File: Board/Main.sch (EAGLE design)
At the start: 1 part

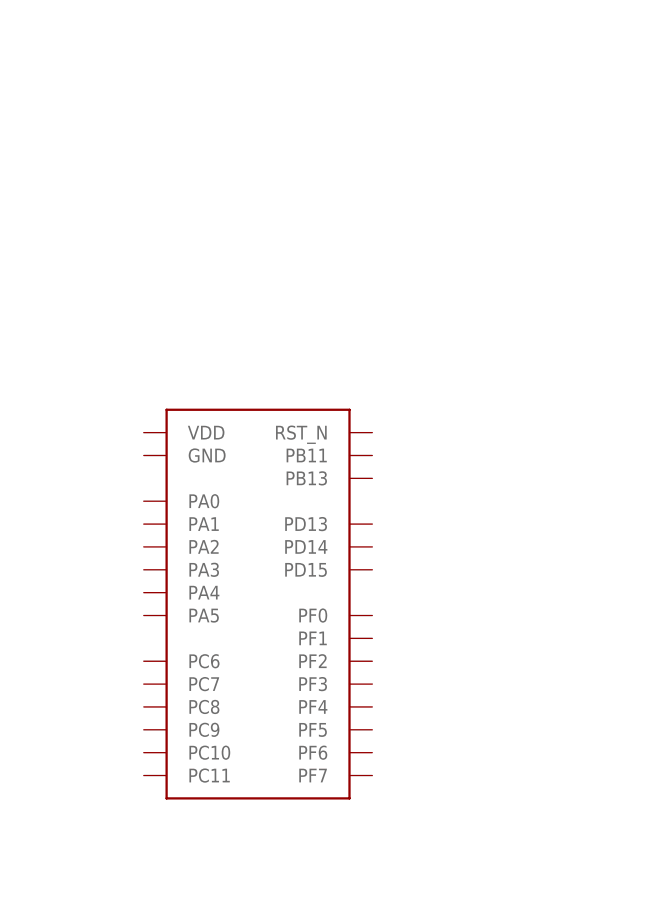
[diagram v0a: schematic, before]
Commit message: Add battery managment
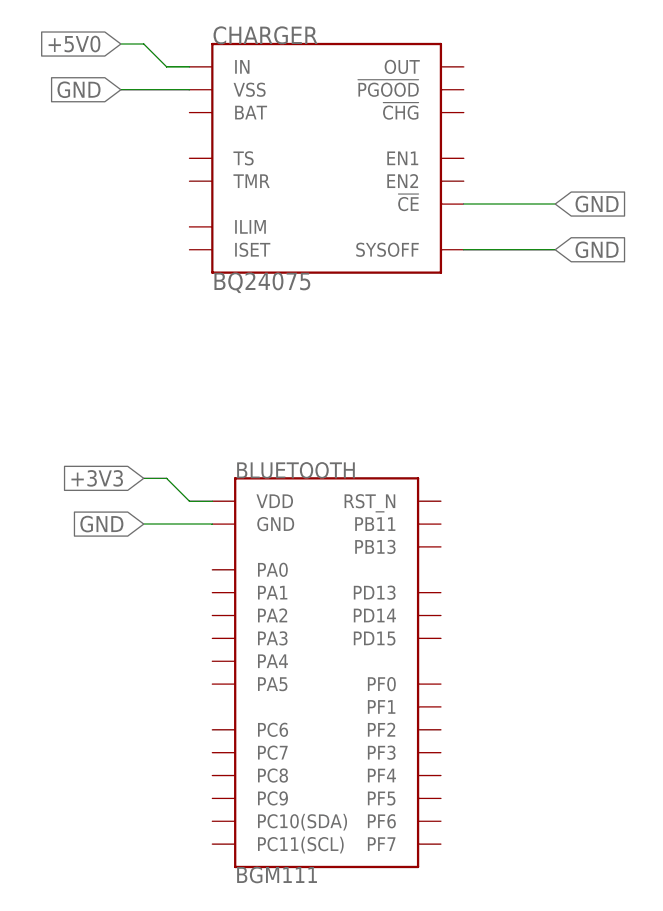
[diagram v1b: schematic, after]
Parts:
- removed BGM111: BGM111, Main Components:BGM111
- added BLUETOOTH: BGM111, Main Components:BGM111
- added CHARGER: BQ24075, Main Components:BQ24075BQ24075
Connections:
- new net +3V3: BLUETOOTH.VDD
- new net +5V0: CHARGER.IN
- new net GND: BLUETOOTH.GND, CHARGER.!CE, CHARGER.SYSOFF, CHARGER.VSS
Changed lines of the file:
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@@
 </classes>
 <parts>
-<part name="BGM111" library="Main Components" deviceset="BGM111" device="" value="BGM111"/>
+<part name="CHARGER" library="Main Components" deviceset="BQ24075" device="BQ24075" value="BQ24075"/>
+<part name="BLUETOOTH" library="Main Components" deviceset="BGM111" device="" value="BGM111"/>
 </parts>
 <sheets>
@@
 </plain>
 <instances>
-<instance part="BGM111" gate="BLUETOOTH" x="48.26" y="58.42" smashed="yes"/>
+<instance part="CHARGER" gate="CHARGER" x="55.88" y="106.68" smashed="yes">
+<attribute name="NAME" x="43.18" y="119.38" size="1.9304" layer="95" font="vector"/>
+<attribute name="VALUE" x="43.18" y="93.98" size="1.9304" layer="96" font="vector" align="top-left"/>
+</instance>
+<instance part="BLUETOOTH" gate="BLUETOOTH" x="55.88" y="50.8" smashed="yes">
+<attribute name="NAME" x="45.72" y="71.12" size="1.778" layer="95" font="vector"/>
+<attribute name="VALUE" x="45.72" y="27.94" size="1.778" layer="96" font="vector" align="top-left"/>
+</instance>
 </instances>
 <busses>
 </busses>
 <nets>
+<net name="GND" class="0">
+<segment>
+<pinref part="BLUETOOTH" gate="BLUETOOTH" pin="GND"/>
+<wire x1="43.18" y1="66.04" x2="35.56" y2="66.04" width="0.1524" layer="91"/>
+<label x="35.56" y="66.04" size="1.778" layer="95" rot="R180" xref="yes"/>
+</segment>
+<segment>
+<pinref part="CHARGER" gate="CHARGER" pin="VSS"/>
+<wire x1="40.64" y1="114.3" x2="33.02" y2="114.3" width="0.1524" layer="91"/>
+<label x="33.02" y="114.3" size="1.778" layer="95" rot="R180" xref="yes"/>
+</segment>
+<segment>
+<pinref part="CHARGER" gate="CHARGER" pin="!CE"/>
+<wire x1="71.12" y1="101.6" x2="81.28" y2="101.6" width="0.1524" layer="91"/>
+<label x="81.28" y="101.6" size="1.778" layer="95" xref="yes"/>
+</segment>
+<segment>
+<pinref part="CHARGER" gate="CHARGER" pin="SYSOFF"/>
+<wire x1="71.12" y1="96.52" x2="81.28" y2="96.52" width="0.1524" layer="91"/>
+<label x="81.28" y="96.52" size="1.778" layer="95" xref="yes"/>
+</segment>
+</net>
+<net name="+3V3" class="0">
+<segment>
+<pinref part="BLUETOOTH" gate="BLUETOOTH" pin="VDD"/>
+<wire x1="43.18" y1="68.58" x2="40.64" y2="68.58" width="0.1524" layer="91"/>
+<wire x1="40.64" y1="68.58" x2="38.1" y2="71.12" width="0.1524" layer="91"/>
+<wire x1="38.1" y1="71.12" x2="35.56" y2="71.12" width="0.1524" layer="91"/>
+<label x="35.56" y="71.12" size="1.778" layer="95" rot="R180" xref="yes"/>
+</segment>
+</net>
+<net name="+5V0" class="0">
+<segment>
+<pinref part="CHARGER" gate="CHARGER" pin="IN"/>
+<wire x1="40.64" y1="116.84" x2="38.1" y2="116.84" width="0.1524" layer="91"/>
+<wire x1="38.1" y1="116.84" x2="35.56" y2="119.38" width="0.1524" layer="91"/>
+<wire x1="35.56" y1="119.38" x2="33.02" y2="119.38" width="0.1524" layer="91"/>
+<label x="33.02" y="119.38" size="1.778" layer="95" rot="R180" xref="yes"/>
+</segment>
+</net>
 </nets>
 </sheet>

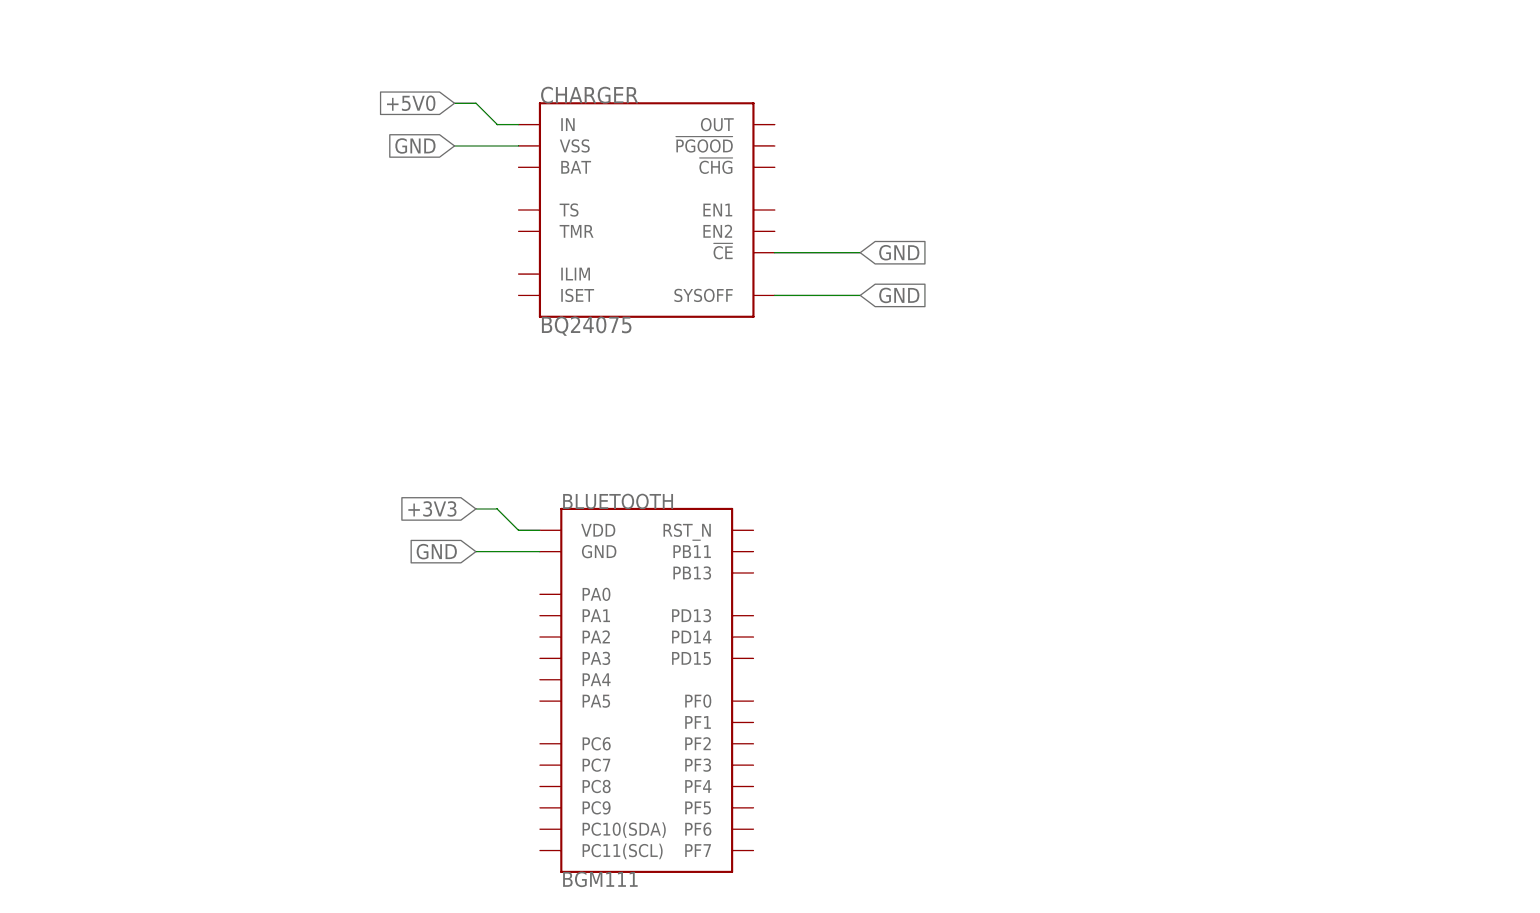
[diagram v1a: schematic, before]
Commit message: Add motor driver
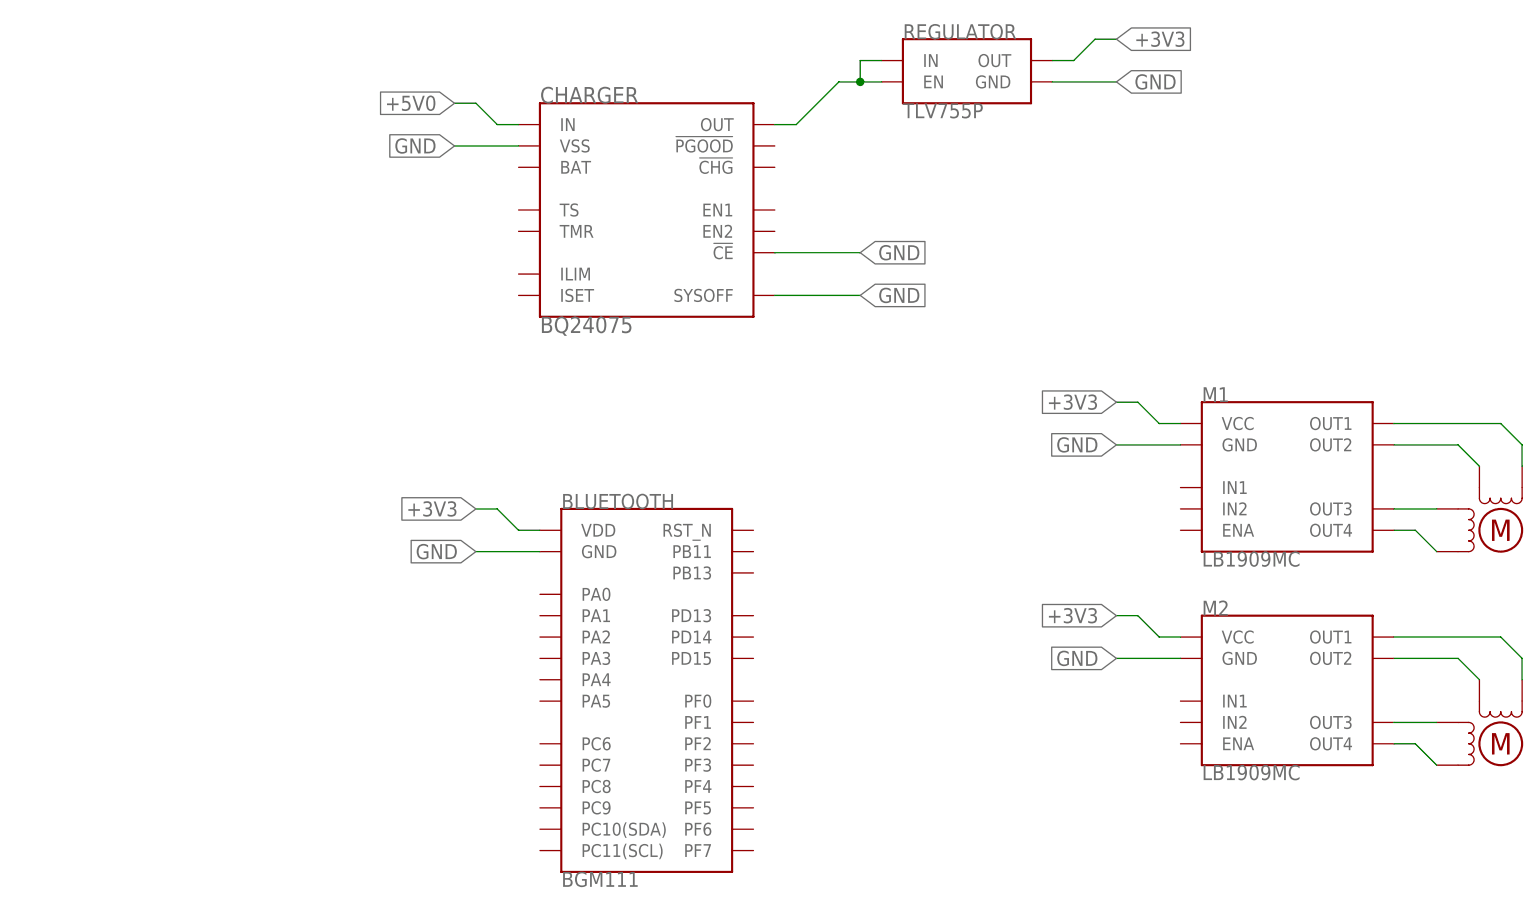
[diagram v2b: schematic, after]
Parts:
- added M1, M2: LB1909MC, Components:LB1909MC
- added REGULATOR: TLV755P, Components:TLV755P
- added U$3, U$4: MOTOR, Components:MOTOR
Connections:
- new net N$1: CHARGER.OUT, REGULATOR.EN, REGULATOR.IN
- new net N$2: M1.OUT4, U$4.P$2
- new net N$3: M2.OUT4, U$3.P$2
- new net N$4: M2.OUT3, U$3.P$1
- new net N$5: M1.OUT3, U$4.P$1
- new net N$6: M1.OUT2, U$4.P$3
- new net N$7: M1.OUT1, U$4.P$4
- new net N$8: M2.OUT2, U$3.P$3
- new net N$9: M2.OUT1, U$3.P$4
- net +3V3: now also M1.VCC, M2.VCC, REGULATOR.OUT
- net GND: now also M1.GND, M2.GND, REGULATOR.GND
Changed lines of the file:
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@@
 <setting verticaltext="up"/>
 </settings>
-<grid distance="0.1" unitdist="inch" unit="inch" style="lines" multiple="1" display="no" altdistance="0.01" altunitdist="inch" altunit="inch"/>
+<grid distance="0.1" unitdist="inch" unit="inch" style="lines" multiple="1" display="yes" altdistance="0.01" altunitdist="inch" altunit="inch"/>
 <layers>
 <layer number="1" name="Top" color="4" fill="1" visible="no" active="no"/>
@@
 <part name="CHARGER" library="Main Components" deviceset="BQ24075" device="BQ24075" value="BQ24075"/>
 <part name="BLUETOOTH" library="Main Components" deviceset="BGM111" device="" value="BGM111"/>
+<part name="REGULATOR" library="Components" deviceset="TLV755P" device="" value="TLV755P"/>
+<part name="M1" library="Components" deviceset="LB1909MC" device=""/>
+<part name="M2" library="Components" deviceset="LB1909MC" device=""/>
+<part name="U$3" library="Components" deviceset="MOTOR" device=""/>
+<part name="U$4" library="Components" deviceset="MOTOR" device=""/>
 </parts>
 <sheets>
@@
 <attribute name="VALUE" x="45.72" y="27.94" size="1.778" layer="96" font="vector" align="top-left"/>
 </instance>
+<instance part="REGULATOR" gate="REGULATOR" x="93.98" y="121.92" smashed="yes">
+<attribute name="NAME" x="86.36" y="127" size="1.778" layer="95" font="vector"/>
+<attribute name="VALUE" x="86.36" y="119.38" size="1.778" layer="96" font="vector" align="top-left"/>
+</instance>
+<instance part="M1" gate="G$1" x="132.08" y="73.66" smashed="yes">
+<attribute name="NAME" x="121.92" y="83.82" size="1.778" layer="95" font="vector"/>
+<attribute name="VALUE" x="121.92" y="66.04" size="1.778" layer="96" font="vector" align="top-left"/>
+</instance>
+<instance part="M2" gate="G$1" x="132.08" y="48.26" smashed="yes">
+<attribute name="NAME" x="121.92" y="58.42" size="1.778" layer="95" font="vector"/>
+<attribute name="VALUE" x="121.92" y="40.64" size="1.778" layer="96" font="vector" align="top-left"/>
+</instance>
+<instance part="U$3" gate="G$1" x="157.48" y="43.18" smashed="yes"/>
+<instance part="U$4" gate="G$1" x="157.48" y="68.58" smashed="yes"/>
 </instances>
 <busses>
@@
 <label x="81.28" y="96.52" size="1.778" layer="95" xref="yes"/>
 </segment>
+<segment>
+<pinref part="REGULATOR" gate="REGULATOR" pin="GND"/>
+<wire x1="104.14" y1="121.92" x2="111.76" y2="121.92" width="0.1524" layer="91"/>
+<label x="111.76" y="121.92" size="1.778" layer="95" xref="yes"/>
+</segment>
+<segment>
+<pinref part="M1" gate="G$1" pin="GND"/>
+<wire x1="119.38" y1="78.74" x2="111.76" y2="78.74" width="0.1524" layer="91"/>
+<label x="111.76" y="78.74" size="1.778" layer="95" rot="R180" xref="yes"/>
+</segment>
+<segment>
+<pinref part="M2" gate="G$1" pin="GND"/>
+<wire x1="119.38" y1="53.34" x2="111.76" y2="53.34" width="0.1524" layer="91"/>
+<label x="111.76" y="53.34" size="1.778" layer="95" rot="R180" xref="yes"/>
+</segment>
 </net>
 <net name="+3V3" class="0">
@@
 <label x="35.56" y="71.12" size="1.778" layer="95" rot="R180" xref="yes"/>
 </segment>
+<segment>
+<pinref part="REGULATOR" gate="REGULATOR" pin="OUT"/>
+<wire x1="104.14" y1="124.46" x2="106.68" y2="124.46" width="0.1524" layer="91"/>
+<wire x1="106.68" y1="124.46" x2="109.22" y2="127" width="0.1524" layer="91"/>
+<wire x1="109.22" y1="127" x2="111.76" y2="127" width="0.1524" layer="91"/>
+<label x="111.76" y="127" size="1.778" layer="95" xref="yes"/>
+</segment>
+<segment>
+<pinref part="M1" gate="G$1" pin="VCC"/>
+<wire x1="119.38" y1="81.28" x2="116.84" y2="81.28" width="0.1524" layer="91"/>
+<wire x1="116.84" y1="81.28" x2="114.3" y2="83.82" width="0.1524" layer="91"/>
+<wire x1="114.3" y1="83.82" x2="111.76" y2="83.82" width="0.1524" layer="91"/>
+<label x="111.76" y="83.82" size="1.778" layer="95" rot="R180" xref="yes"/>
+</segment>
+<segment>
+<pinref part="M2" gate="G$1" pin="VCC"/>
+<wire x1="119.38" y1="55.88" x2="116.84" y2="55.88" width="0.1524" layer="91"/>
+<wire x1="116.84" y1="55.88" x2="114.3" y2="58.42" width="0.1524" layer="91"/>
+<wire x1="114.3" y1="58.42" x2="111.76" y2="58.42" width="0.1524" layer="91"/>
+<label x="111.76" y="58.42" size="1.778" layer="95" rot="R180" xref="yes"/>
+</segment>
 </net>
 <net name="+5V0" class="0">
@@
 </segment>
 </net>
+<net name="N$1" class="0">
+<segment>
+<pinref part="REGULATOR" gate="REGULATOR" pin="IN"/>
+<pinref part="REGULATOR" gate="REGULATOR" pin="EN"/>
+<wire x1="81.28" y1="124.46" x2="83.82" y2="124.46" width="0.1524" layer="91"/>
+<wire x1="83.82" y1="121.92" x2="81.28" y2="121.92" width="0.1524" layer="91"/>
+<wire x1="81.28" y1="121.92" x2="81.28" y2="124.46" width="0.1524" layer="91"/>
+<wire x1="81.28" y1="121.92" x2="78.74" y2="121.92" width="0.1524" layer="91"/>
+<junction x="81.28" y="121.92"/>
+<wire x1="78.74" y1="121.92" x2="73.66" y2="116.84" width="0.1524" layer="91"/>
+<pinref part="CHARGER" gate="CHARGER" pin="OUT"/>
+<wire x1="73.66" y1="116.84" x2="71.12" y2="116.84" width="0.1524" layer="91"/>
+</segment>
+</net>
+<net name="N$2" class="0">
+<segment>
+<pinref part="M1" gate="G$1" pin="OUT4"/>
+<wire x1="144.78" y1="68.58" x2="147.32" y2="68.58" width="0.1524" layer="91"/>
+<wire x1="147.32" y1="68.58" x2="149.86" y2="66.04" width="0.1524" layer="91"/>
+<pinref part="U$4" gate="G$1" pin="P$2"/>
+</segment>
+</net>
+<net name="N$3" class="0">
+<segment>
+<pinref part="M2" gate="G$1" pin="OUT4"/>
+<wire x1="144.78" y1="43.18" x2="147.32" y2="43.18" width="0.1524" layer="91"/>
+<wire x1="147.32" y1="43.18" x2="149.86" y2="40.64" width="0.1524" layer="91"/>
+<pinref part="U$3" gate="G$1" pin="P$2"/>
+</segment>
+</net>
+<net name="N$4" class="0">
+<segment>
+<pinref part="M2" gate="G$1" pin="OUT3"/>
+<pinref part="U$3" gate="G$1" pin="P$1"/>
+<wire x1="144.78" y1="45.72" x2="149.86" y2="45.72" width="0.1524" layer="91"/>
+</segment>
+</net>
+<net name="N$5" class="0">
+<segment>
+<pinref part="M1" gate="G$1" pin="OUT3"/>
+<pinref part="U$4" gate="G$1" pin="P$1"/>
+<wire x1="144.78" y1="71.12" x2="149.86" y2="71.12" width="0.1524" layer="91"/>
+</segment>
+</net>
+<net name="N$6" class="0">
+<segment>
+<pinref part="U$4" gate="G$1" pin="P$3"/>
+<wire x1="154.94" y1="76.2" x2="152.4" y2="78.74" width="0.1524" layer="91"/>
+<pinref part="M1" gate="G$1" pin="OUT2"/>
+<wire x1="152.4" y1="78.74" x2="144.78" y2="78.74" width="0.1524" layer="91"/>
+</segment>
+</net>
+<net name="N$7" class="0">
+<segment>
+<pinref part="M1" gate="G$1" pin="OUT1"/>
+<wire x1="144.78" y1="81.28" x2="157.48" y2="81.28" width="0.1524" layer="91"/>
+<wire x1="157.48" y1="81.28" x2="160.02" y2="78.74" width="0.1524" layer="91"/>
+<pinref part="U$4" gate="G$1" pin="P$4"/>
+<wire x1="160.02" y1="78.74" x2="160.02" y2="76.2" width="0.1524" layer="91"/>
+</segment>
+</net>
+<net name="N$8" class="0">
+<segment>
+<pinref part="M2" gate="G$1" pin="OUT2"/>
+<wire x1="144.78" y1="53.34" x2="152.4" y2="53.34" width="0.1524" layer="91"/>
+<pinref part="U$3" gate="G$1" pin="P$3"/>
+<wire x1="152.4" y1="53.34" x2="154.94" y2="50.8" width="0.1524" layer="91"/>
+</segment>
+</net>
+<net name="N$9" class="0">
+<segment>
+<pinref part="M2" gate="G$1" pin="OUT1"/>
+<wire x1="144.78" y1="55.88" x2="157.48" y2="55.88" width="0.1524" layer="91"/>
+<wire x1="157.48" y1="55.88" x2="160.02" y2="53.34" width="0.1524" layer="91"/>
+<pinref part="U$3" gate="G$1" pin="P$4"/>
+<wire x1="160.02" y1="53.34" x2="160.02" y2="50.8" width="0.1524" layer="91"/>
+</segment>
+</net>
